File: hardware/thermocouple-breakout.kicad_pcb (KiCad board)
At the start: 2 copper layers, 36.8 x 56.8 mm, 15 parts, among them P1 CONN_4, P2 CONN_2, U1 AD594/95, U2 74HCT04

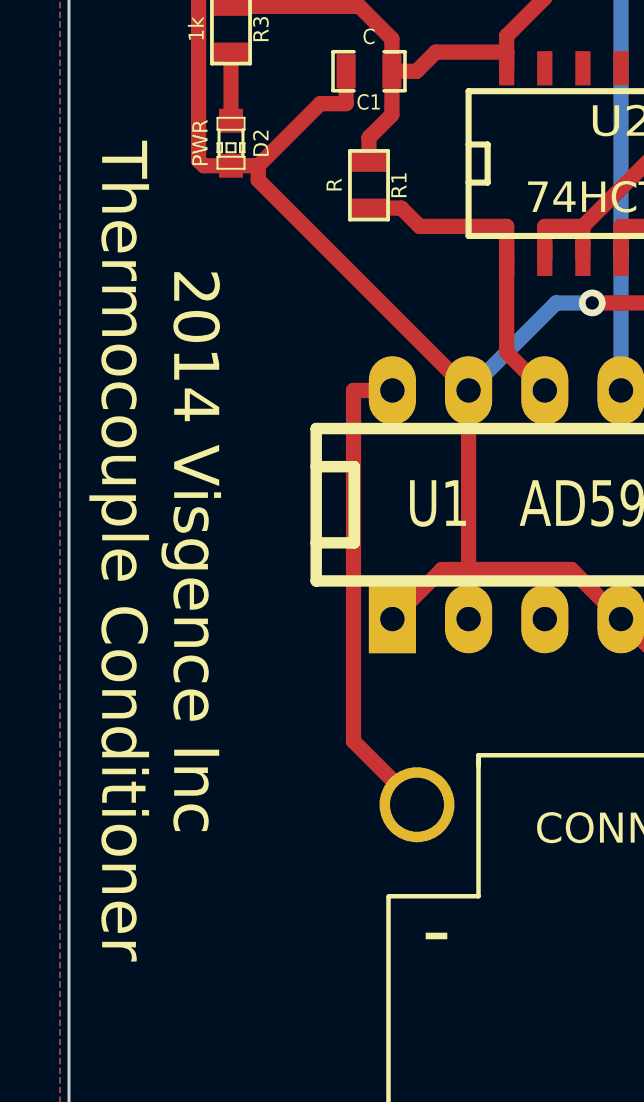
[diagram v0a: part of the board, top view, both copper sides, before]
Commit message: Updated to kicad 4.0.2
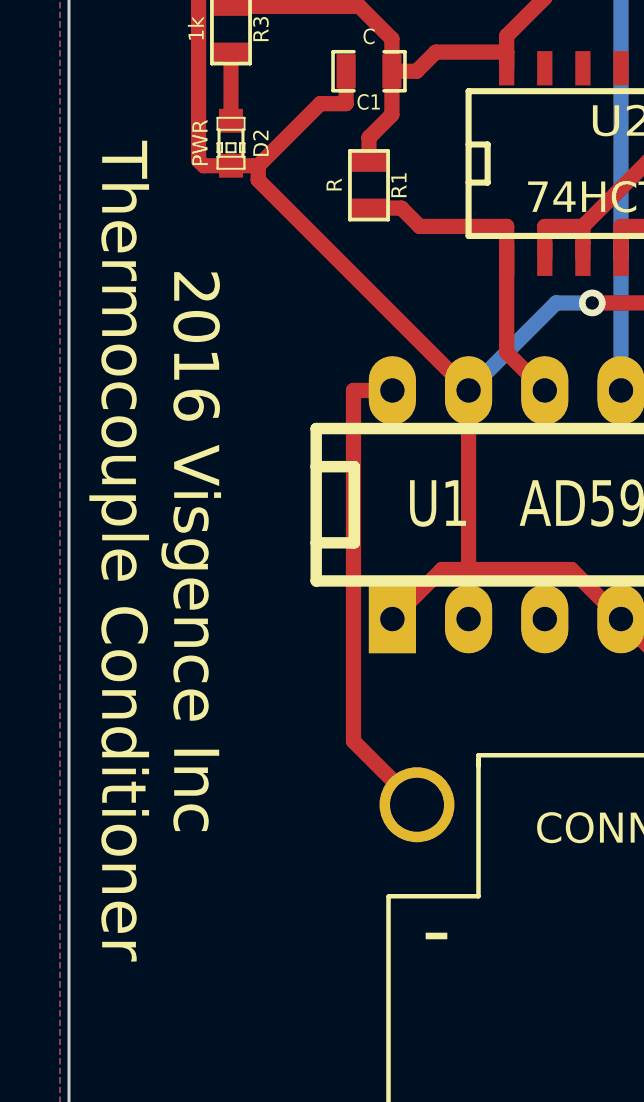
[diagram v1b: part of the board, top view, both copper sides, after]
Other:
- board text added: "2016 Visgence Inc"
- board text removed: "2014 Visgence Inc"
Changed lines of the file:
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@@
-(kicad_pcb (version 3) (host pcbnew "(2014-03-07 BZR 4737)-product")
+(kicad_pcb (version 4) (host pcbnew 4.0.2-stable)
   (general
     (links 25)
     (no_connects 0)
-    (area 38.5 30.792 78.021648 91.500001)
+    (area 38.749999 33.944122 75.650001 90.855878)
     (thickness 1.6)
     (drawings 14)
@@
   (page A4)
   (layers
-    (15 F.Cu signal)
-    (0 B.Cu signal)
-    (16 B.Adhes user)
-    (17 F.Adhes user)
-    (18 B.Paste user)
-    (19 F.Paste user)
-    (20 B.SilkS user)
-    (21 F.SilkS user)
-    (22 B.Mask user)
-    (23 F.Mask user)
-    (24 Dwgs.User user)
-    (25 Cmts.User user)
-    (26 Eco1.User user)
-    (27 Eco2.User user)
-    (28 Edge.Cuts user)
+    (0 F.Cu signal)
+    (31 B.Cu signal)
+    (32 B.Adhes user)
+    (33 F.Adhes user)
+    (34 B.Paste user)
+    (35 F.Paste user)
+    (36 B.SilkS user)
+    (37 F.SilkS user)
+    (38 B.Mask user)
+    (39 F.Mask user)
+    (40 Dwgs.User user)
+    (41 Cmts.User user)
+    (42 Eco1.User user)
+    (43 Eco2.User user)
+    (44 Edge.Cuts user)
   )
   (setup
@@
     (pad_drill 3.5)
     (pad_to_mask_clearance 0)
-    (aux_axis_origin 0 0)
+    (aux_axis_origin 38.8 34)
     (visible_elements 7FFFFF7F)
     (pcbplotparams
-      (layerselection 283148289)
+      (layerselection 0x010f0_80000001)
       (usegerberextensions true)
       (excludeedgelayer false)
@@
       (viasonmask false)
       (mode 1)
-      (useauxorigin false)
+      (useauxorigin true)
       (hpglpennumber 1)
       (hpglpenspeed 20)
@@
       (plotreference true)
       (plotvalue true)
-      (plotothertext true)
       (plotinvisibletext false)
       (padsonsilk false)
@@
     (uvia_dia 0.508)
     (uvia_drill 0.127)
-    (add_net "")
     (add_net ALARM)
     (add_net GND)
@@
     (effects (font (size 1.5 1.5) (thickness 0.3)))
   )
-  (gr_text "2014 Visgence Inc" (at 43 63.2 270) (layer F.SilkS)
+  (gr_text "2016 Visgence Inc" (at 43 63.2 270) (layer F.SilkS)
     (effects (font (size 1.5 1.5) (thickness 0.3)))
   )
